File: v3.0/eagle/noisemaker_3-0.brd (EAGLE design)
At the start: 76.3 x 66.9 mm, 57 parts, among them IC1 REG1117

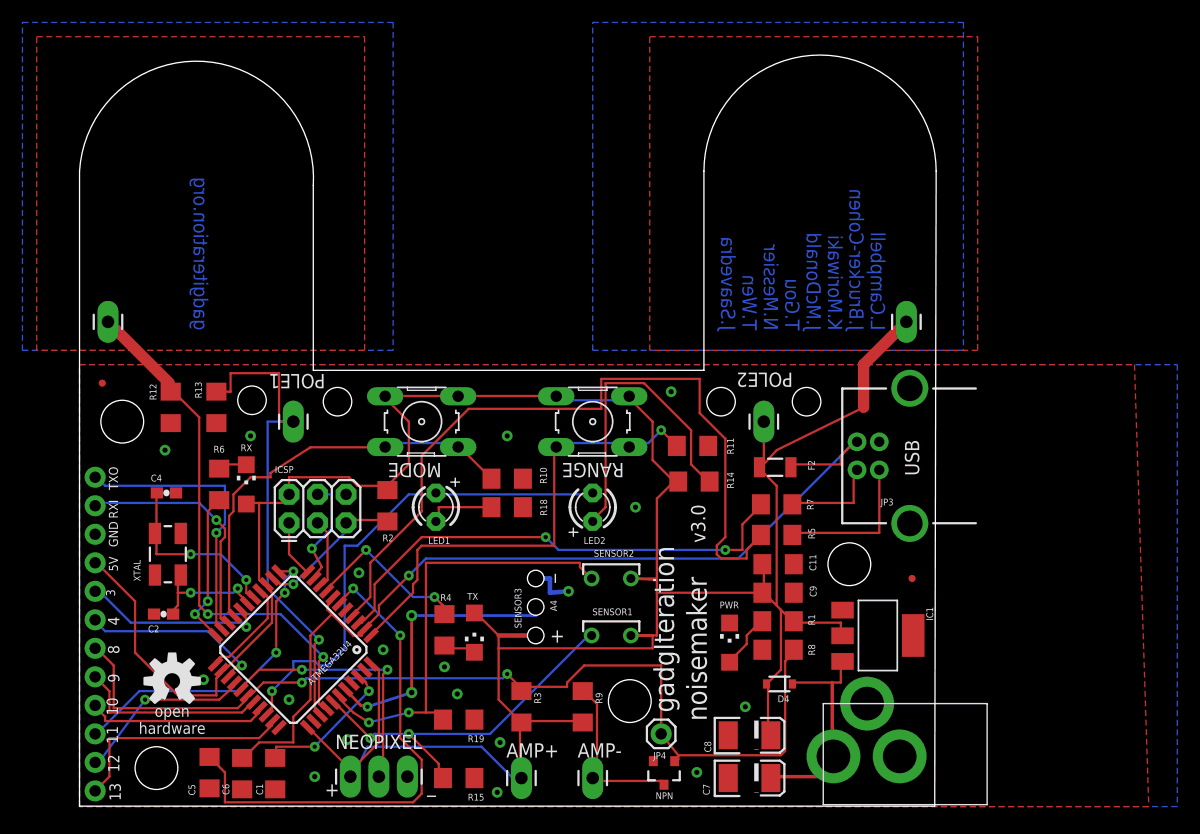
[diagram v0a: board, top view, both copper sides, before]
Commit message: fixed critical outline error
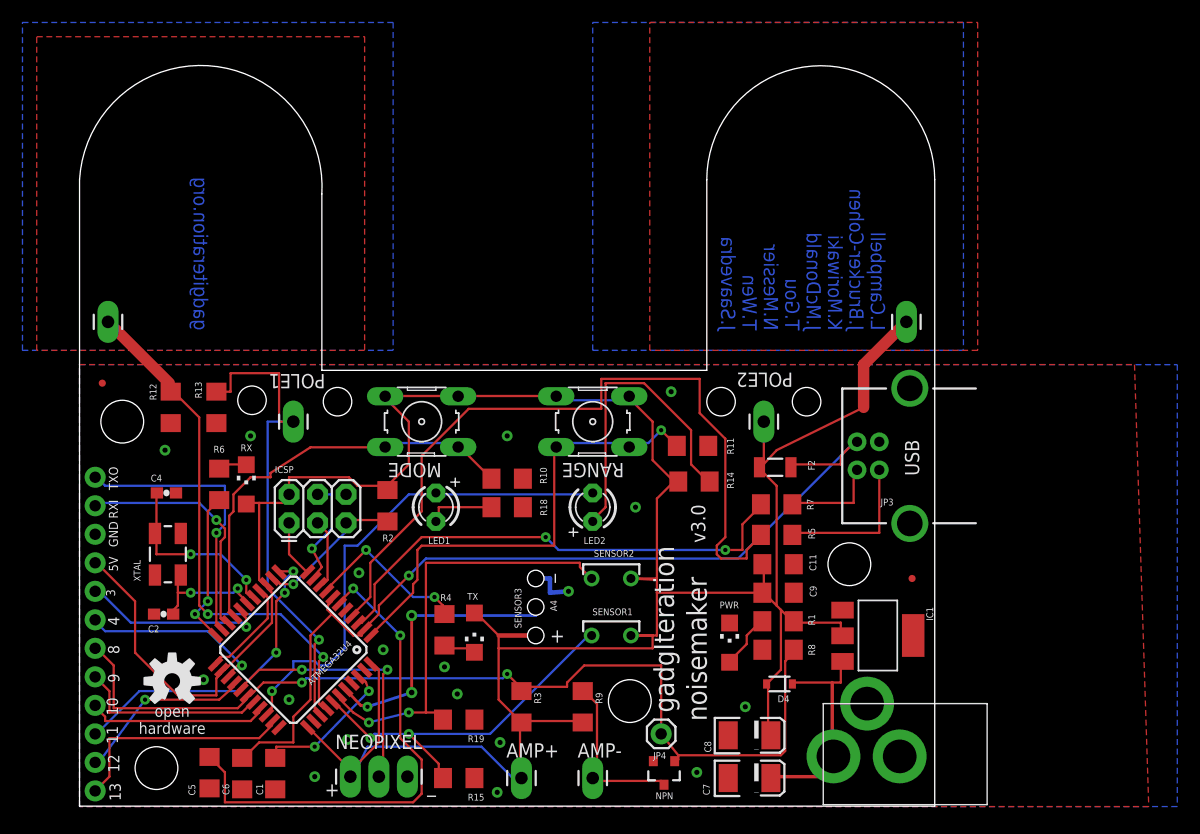
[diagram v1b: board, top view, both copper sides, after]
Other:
- board size 76.3 x 66.9 mm -> 76.2 x 66 mm
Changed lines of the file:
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@@
 <layer number="18" name="Vias" color="2" fill="1" visible="yes" active="yes"/>
 <layer number="19" name="Unrouted" color="6" fill="1" visible="no" active="yes"/>
-<layer number="20" name="Dimension" color="15" fill="1" visible="no" active="yes"/>
+<layer number="20" name="Dimension" color="15" fill="1" visible="yes" active="yes"/>
 <layer number="21" name="tPlace" color="16" fill="1" visible="yes" active="yes"/>
 <layer number="22" name="bPlace" color="14" fill="1" visible="no" active="yes"/>
@@
 <layer number="27" name="tValues" color="7" fill="1" visible="no" active="yes"/>
 <layer number="28" name="bValues" color="7" fill="1" visible="no" active="yes"/>
-<layer number="29" name="tStop" color="7" fill="3" visible="yes" active="yes"/>
-<layer number="30" name="bStop" color="7" fill="6" visible="yes" active="yes"/>
+<layer number="29" name="tStop" color="7" fill="3" visible="no" active="yes"/>
+<layer number="30" name="bStop" color="7" fill="6" visible="no" active="yes"/>
 <layer number="31" name="tCream" color="7" fill="4" visible="no" active="yes"/>
 <layer number="32" name="bCream" color="7" fill="5" visible="no" active="yes"/>
@@
 <layer number="43" name="vRestrict" color="2" fill="10" visible="no" active="yes"/>
 <layer number="44" name="Drills" color="7" fill="1" visible="no" active="yes"/>
-<layer number="45" name="Holes" color="7" fill="1" visible="yes" active="yes"/>
+<layer number="45" name="Holes" color="7" fill="1" visible="no" active="yes"/>
 <layer number="46" name="Milling" color="3" fill="1" visible="no" active="yes"/>
 <layer number="47" name="Measures" color="7" fill="1" visible="no" active="yes"/>
 <layer number="48" name="Document" color="7" fill="1" visible="yes" active="yes"/>
-<layer number="49" name="Reference" color="7" fill="1" visible="no" active="yes"/>
+<layer number="49" name="Reference" color="7" fill="1" visible="yes" active="yes"/>
 <layer number="50" name="dxf" color="7" fill="1" visible="no" active="yes"/>
 <layer number="51" name="tDocu" color="6" fill="1" visible="no" active="yes"/>
@@
 </polygon>
 <wire x1="0.005" y1="0.038" x2="76.185" y2="0.038" width="0" layer="20"/>
-<wire x1="76.185" y1="0.038" x2="76.312" y2="56.604" width="0" layer="20"/>
-<wire x1="76.312" y1="56.604" x2="55.626" y2="56.604" width="0" layer="20" curve="180"/>
-<wire x1="55.626" y1="56.604" x2="55.626" y2="38.862" width="0" layer="20"/>
-<wire x1="55.626" y1="38.862" x2="20.828" y2="38.862" width="0" layer="20"/>
-<wire x1="20.828" y1="38.862" x2="20.828" y2="55.334" width="0" layer="20"/>
-<wire x1="20.828" y1="55.334" x2="0.005" y2="56.604" width="0" layer="20" curve="180"/>
-<wire x1="0.005" y1="56.604" x2="0.005" y2="0.038" width="0" layer="20"/>
+<wire x1="76.185" y1="0.038" x2="76.185" y2="55.842" width="0" layer="20"/>
+<wire x1="76.185" y1="55.842" x2="55.88" y2="55.842" width="0" layer="20" curve="180"/>
+<wire x1="55.88" y1="55.842" x2="55.88" y2="38.862" width="0" layer="20"/>
+<wire x1="55.88" y1="38.862" x2="21.59" y2="38.862" width="0" layer="20"/>
+<wire x1="21.59" y1="38.862" x2="21.59" y2="54.572" width="0" layer="20"/>
+<wire x1="21.59" y1="54.572" x2="0.005" y2="55.842" width="0" layer="20" curve="180"/>
+<wire x1="0.005" y1="55.842" x2="0.005" y2="0.038" width="0" layer="20"/>
 <rectangle x1="-2.54" y1="40.64" x2="78.74" y2="67.31" layer="29"/>
 <rectangle x1="-3.81" y1="40.64" x2="77.47" y2="68.58" layer="30"/>
@@
 </polygon>
 <polygon width="0.4064" layer="1">
-<vertex x="50.8" y="68.58"/>
-<vertex x="80.01" y="68.58"/>
+<vertex x="50.8" y="69.85"/>
+<vertex x="80.01" y="69.85"/>
 <vertex x="80.01" y="40.64"/>
 <vertex x="50.8" y="40.64"/>

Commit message: small adjustments, this is final board
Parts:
- R14, R18: value (none) -> 330
- R15, R19: value (none) -> 10k
- R3, R8: value (none) -> 1M
- R9: value (none) -> 22k
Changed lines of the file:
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@@
 <attribute name="VALUE" x="63.627" y="23.114" size="0.4064" layer="27" rot="R180"/>
 </element>
-<element name="R3" library="SparkFun-Passives" package="1206" value="" x="39.37" y="8.89" smashed="yes" rot="R270">
+<element name="R3" library="SparkFun-Passives" package="1206" value="1M" x="39.37" y="8.89" smashed="yes" rot="R270">
 <attribute name="NAME" x="40.513" y="10.16" size="0.6096" layer="25" rot="R270"/>
 <attribute name="VALUE" x="37.846" y="10.287" size="0.4064" layer="27" rot="R270"/>
 </element>
-<element name="R8" library="SparkFun-Passives" package="1206" value="" x="62.23" y="13.97" smashed="yes">
+<element name="R8" library="SparkFun-Passives" package="1206" value="1M" x="62.23" y="13.97" smashed="yes">
 <attribute name="NAME" x="65.532" y="13.462" size="0.6096" layer="25" rot="R90"/>
 <attribute name="VALUE" x="60.833" y="12.446" size="0.4064" layer="27"/>
 </element>
-<element name="R9" library="SparkFun-Passives" package="1206" value="" x="44.831" y="8.89" smashed="yes" rot="R270">
+<element name="R9" library="SparkFun-Passives" package="1206" value="22k" x="44.831" y="8.89" smashed="yes" rot="R270">
 <attribute name="NAME" x="45.974" y="10.16" size="0.6096" layer="25" rot="R270"/>
 <attribute name="VALUE" x="43.307" y="10.287" size="0.4064" layer="27" rot="R270"/>
@@
 <attribute name="VALUE" x="50.546" y="13.97" size="1.27" layer="27" rot="R180"/>
 </element>
-<element name="R15" library="SparkFun-Passives" package="1206" value="" x="33.782" y="2.54" smashed="yes" rot="R180">
+<element name="R15" library="SparkFun-Passives" package="1206" value="10k" x="33.782" y="2.54" smashed="yes" rot="R180">
 <attribute name="NAME" x="36.068" y="1.143" size="0.6096" layer="25" rot="R180"/>
 <attribute name="VALUE" x="35.179" y="4.064" size="0.4064" layer="27" rot="R180"/>
 </element>
-<element name="R19" library="SparkFun-Passives" package="1206" value="" x="33.782" y="7.747" smashed="yes" rot="R180">
+<element name="R19" library="SparkFun-Passives" package="1206" value="10k" x="33.782" y="7.747" smashed="yes" rot="R180">
 <attribute name="NAME" x="36.068" y="6.35" size="0.6096" layer="25" rot="R180"/>
 <attribute name="VALUE" x="35.179" y="9.271" size="0.4064" layer="27" rot="R180"/>
@@
 <attribute name="VALUE" x="47.371" y="28.575" size="1.27" layer="27" ratio="10" rot="R90"/>
 </element>
-<element name="R14" library="SparkFun-Passives" package="1206" value="" x="54.737" y="28.956" smashed="yes">
+<element name="R14" library="SparkFun-Passives" package="1206" value="330" x="54.737" y="28.956" smashed="yes">
 <attribute name="NAME" x="58.293" y="28.321" size="0.6096" layer="25" rot="R90"/>
 <attribute name="VALUE" x="53.34" y="27.432" size="0.4064" layer="27"/>
 </element>
-<element name="R18" library="SparkFun-Passives" package="1206" value="" x="38.1" y="26.67" smashed="yes">
+<element name="R18" library="SparkFun-Passives" package="1206" value="330" x="38.1" y="26.67" smashed="yes">
 <attribute name="NAME" x="41.656" y="25.908" size="0.6096" layer="25" rot="R90"/>
 <attribute name="VALUE" x="36.703" y="25.146" size="0.4064" layer="27"/>

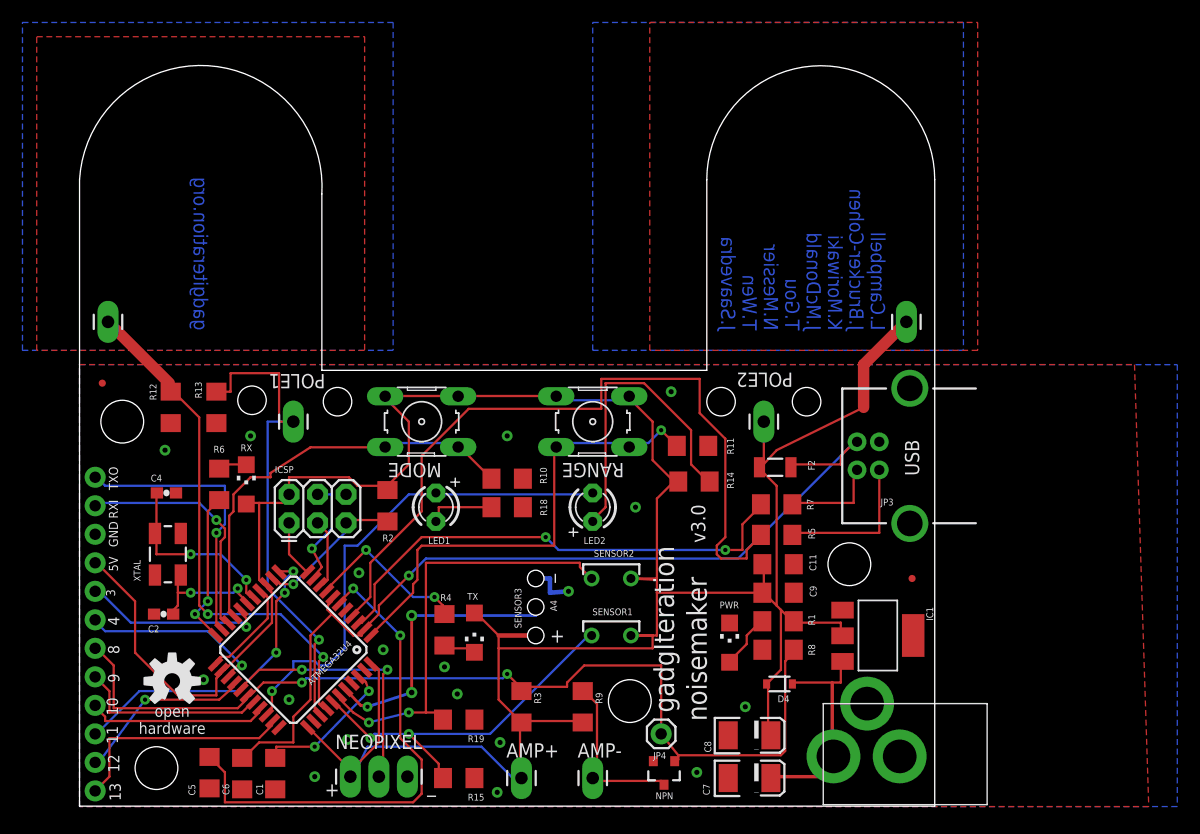
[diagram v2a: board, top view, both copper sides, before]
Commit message: updated voltage regulator, added second footprint for NPN options
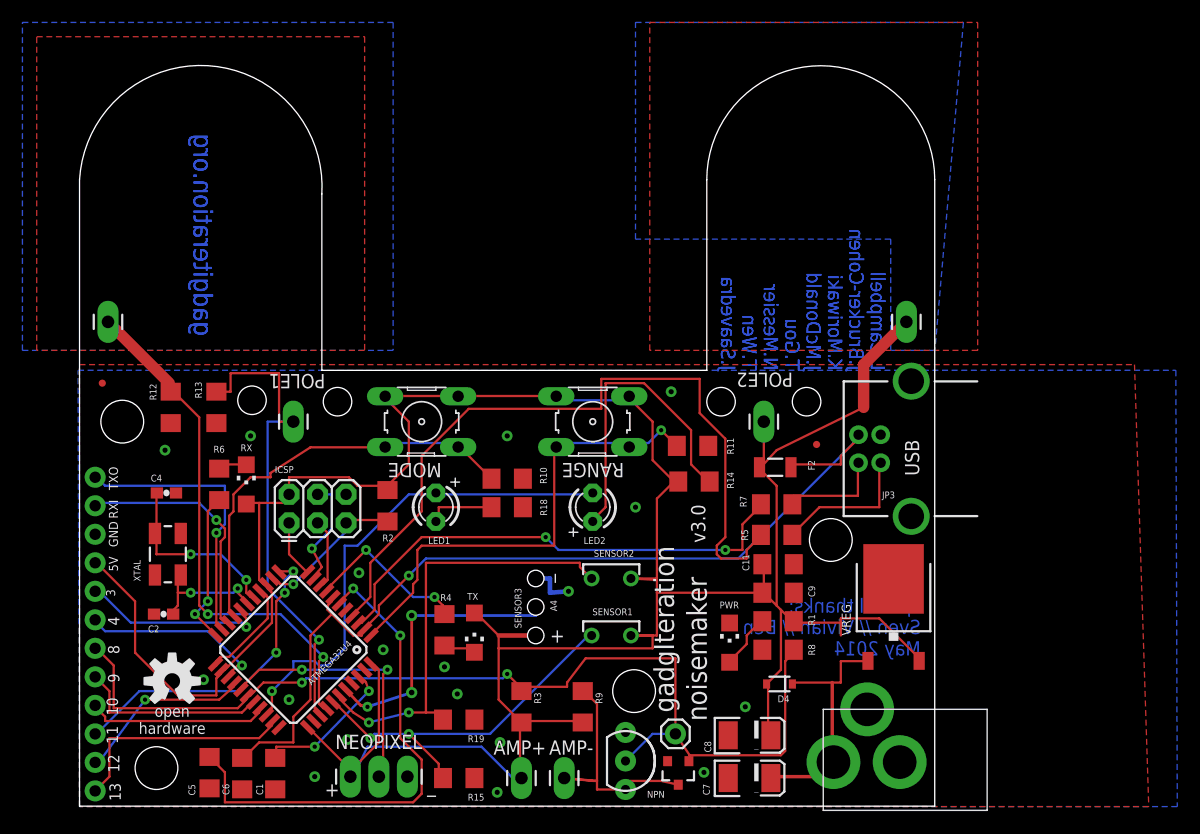
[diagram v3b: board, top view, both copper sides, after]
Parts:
- removed IC1: REG1117, burr-brown:SOT223
- added Q1: (no value), SparkFun-DiscreteSemi:TO-92-AMMO
- added VREG: 7805DT, linear:TO252
- moved JP2 14.7 mm to (65.7, 32.3)
- moved AMP- 2.54 mm to (43.2, 2.54)
- moved NPN 1.27 mm to (53.3, 3.05)
- moved JP4 1.27 mm to (53.1, 6.48)
- moved JP3 0.65 mm to (71.4, 31.9)
- moved U$1 0.51 mm to (76.5, 4.06)
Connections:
- net D8: now also Q1.2
- net GND: now also Q1.1, VREG.3; no longer IC1.1
- net RAW: now also VREG.1; no longer IC1.3
- net SPKR_OUT: now also Q1.3
- net VCC: now also VREG.2; no longer IC1.2
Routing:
- net VCC: track 265.0 -> 273.9 mm
- net SPKR_OUT: track 15.8 -> 23.3 mm
- net D8: track 86.5 -> 92.9 mm
- net RAW: track 20.2 -> 23.1 mm
- net UVCC: track 82.4 -> 83.5 mm
- net N$9: track 8.59 -> 9.44 mm
- net N$8: track 13.4 -> 12.8 mm
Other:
- board text added: "special thanks: Sven // Vivian // Ben May 2014"
